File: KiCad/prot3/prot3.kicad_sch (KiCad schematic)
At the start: 198 parts, among them J1 Conn_01x02_Socket, J2 LED_SW, J3 Conn_01x04_Socket, Q1 Q_Photo_NPN, Q10 Q_Photo_NPN, Q11 Q_Photo_NPN, Q12 Q_Photo_NPN, Q13 Q_Photo_NPN, Q14 Q_Photo_NPN, Q15 Q_Photo_NPN, Q16 Q_Photo_NPN, Q17 Q_Photo_NPN, Q18 Q_Photo_NPN, Q19 Q_Photo_NPN, Q2 Q_Photo_NPN, Q20 Q_Photo_NPN, Q21 Q_Photo_NPN, Q22 Q_Photo_NPN, Q23 Q_Photo_NPN, Q24 Q_Photo_NPN, Q25 Q_Photo_NPN, Q26 Q_Photo_NPN, Q27 Q_Photo_NPN, Q28 Q_Photo_NPN, Q29 Q_Photo_NPN, Q3 Q_Photo_NPN, Q30 Q_Photo_NPN, Q31 Q_Photo_NPN, Q32 Q_Photo_NPN, Q4 Q_Photo_NPN, Q5 Q_Photo_NPN, Q6 Q_Photo_NPN, Q7 Q_Photo_NPN, Q8 Q_Photo_NPN, Q9 Q_Photo_NPN, U1 LM339, U2 LM339, U3 LM339, U4 LM339, U5 LM339, U6 LM339, U7 LM339, U8 LM339

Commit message: コンパレーター割当て途中
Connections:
- net 1A: now also Q31.2 (E), Rs31.1
- net 1B: now also Q32.2 (E), Rs32.1
- net 1C: now also Q2.2 (E), Rs2.1
- net 1D: now also Q1.2 (E), Rs1.1
- net 2A: now also Q4.2 (E), Rs4.1
- net 2B: now also Q3.2 (E), Rs3.1
- net 2C: now also Q6.2 (E), Rs6.1
- net 2D: now also Q5.2 (E), Rs5.1
- net 3A: now also Q7.2 (E), Rs7.1
- net 3B: now also Q8.2 (E), Rs8.1
- net 3C: now also Q10.2 (E), Rs10.1
- net 3D: now also Q9.2 (E), Rs9.1
- net 4A: now also Q11.2 (E), Rs11.1
- net 4B: now also Q12.2 (E), Rs12.1
- net 4C: now also Q14.2 (E), Rs14.1
- net 4D: now also Q13.2 (E), Rs13.1
- net 5A: now also Q15.2 (E), Rs15.1
- net 5B: now also Q16.2 (E), Rs16.1
- net 5D: now also Q17.2 (E), Rs17.1
- net 6A: now also Q18.2 (E), Rs18.1
- net 6B: now also Q19.2 (E), Rs19.1
- net 6D: now also Q20.2 (E), Rs20.1
- net 7A: now also Q21.2 (E), Rs21.1
- net 7B: now also Q22.2 (E), Rs22.1
- net 7C: now also Q24.2 (E), Rs24.1
- net 7D: now also Q23.2 (E), Rs23.1
- net 8A: now also Q25.2 (E), Q28.2 (E), Rs25.1, Rs28.1
- net 8B: now also Q26.2 (E), Q27.2 (E), Rs26.1, Rs27.1
- net 8C: now also Q30.2 (E), Rs30.1
- net 8D: now also Q29.2 (E), Rs29.1
- net GND: no longer C13.1, D1.2 (A), D10.2 (A), D11.2 (A), D12.2 (A), D13.2 (A), D14.2 (A), D15.2 (A), D16.2 (A), D17.2 (A), D18.2 (A), D19.2 (A), D2.2 (A), D20.2 (A), D21.2 (A), D22.2 (A), D23.2 (A), D24.2 (A), D25.2 (A), D26.2 (A), D27.2 (A), D28.2 (A), D29.2 (A), D3.2 (A), D30.2 (A), D31.2 (A), D32.2 (A), D4.2 (A), D5.2 (A), D6.2 (A), D7.2 (A), D8.2 (A), D9.2 (A), J1.1 (Pin_1), J2.3 (Pin_3)
- new net LED_5V: C13.1, D1.2 (A), D10.2 (A), D11.2 (A), D12.2 (A), D13.2 (A), D14.2 (A), D15.2 (A), D16.2 (A), D17.2 (A), D18.2 (A), D19.2 (A), D2.2 (A), D20.2 (A), D21.2 (A), D22.2 (A), D23.2 (A), D24.2 (A), D25.2 (A), D26.2 (A), D27.2 (A), D28.2 (A), D29.2 (A), D3.2 (A), D30.2 (A), D31.2 (A), D32.2 (A), D4.2 (A), D5.2 (A), D6.2 (A), D7.2 (A), D8.2 (A), D9.2 (A), J1.1 (Pin_1), J2.3 (Pin_3)

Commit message: conp+一周、センサーch割当てまで
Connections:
- net 1A: now also Q32.2 (E), Rs32.1; no longer Q31.2 (E), Rs31.1
- net 1B: now also Q31.2 (E), Rs31.1; no longer Q32.2 (E), Rs32.1
- net 3A: now also Q8.2 (E), Rs8.1; no longer Q7.2 (E), Rs7.1
- net 3B: now also Q7.2 (E), Rs7.1; no longer Q8.2 (E), Rs8.1
- net 4A: now also Q12.2 (E), Rs12.1; no longer Q11.2 (E), Rs11.1
- net 4B: now also Q11.2 (E), Rs11.1; no longer Q12.2 (E), Rs12.1
- net 5A: now also Q16.2 (E), Rs16.1; no longer Q15.2 (E), Rs15.1
- net 5B: now also Q15.2 (E), Rs15.1; no longer Q16.2 (E), Rs16.1
- net 5C: now also Q18.2 (E), Rs18.1
- net 6A: now also Q20.2 (E), Rs20.1; no longer Q18.2 (E), Rs18.1
- net 6C: now also Q22.2 (E), Rs22.1
- net 6D: now also Q21.2 (E), Rs21.1; no longer Q20.2 (E), Rs20.1
- net 7A: now also Q24.2 (E), Rs24.1; no longer Q21.2 (E), Rs21.1
- net 7B: now also Q23.2 (E), Rs23.1; no longer Q22.2 (E), Rs22.1
- net 7C: now also Q26.2 (E), Rs26.1; no longer Q24.2 (E), Rs24.1
- net 7D: now also Q25.2 (E), Rs25.1; no longer Q23.2 (E), Rs23.1
- net 8A: no longer Q25.2 (E), Rs25.1
- net 8B: no longer Q26.2 (E), Rs26.1
- net LED_5V: now also J2.1 (Pin_1); no longer J1.1 (Pin_1), J2.3 (Pin_3)
- net at J2.2 (Pin_2): now also J1.1 (Pin_1), J2.3 (Pin_3); no longer J2.1 (Pin_1)
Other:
- moved on the sheet: C13, J2

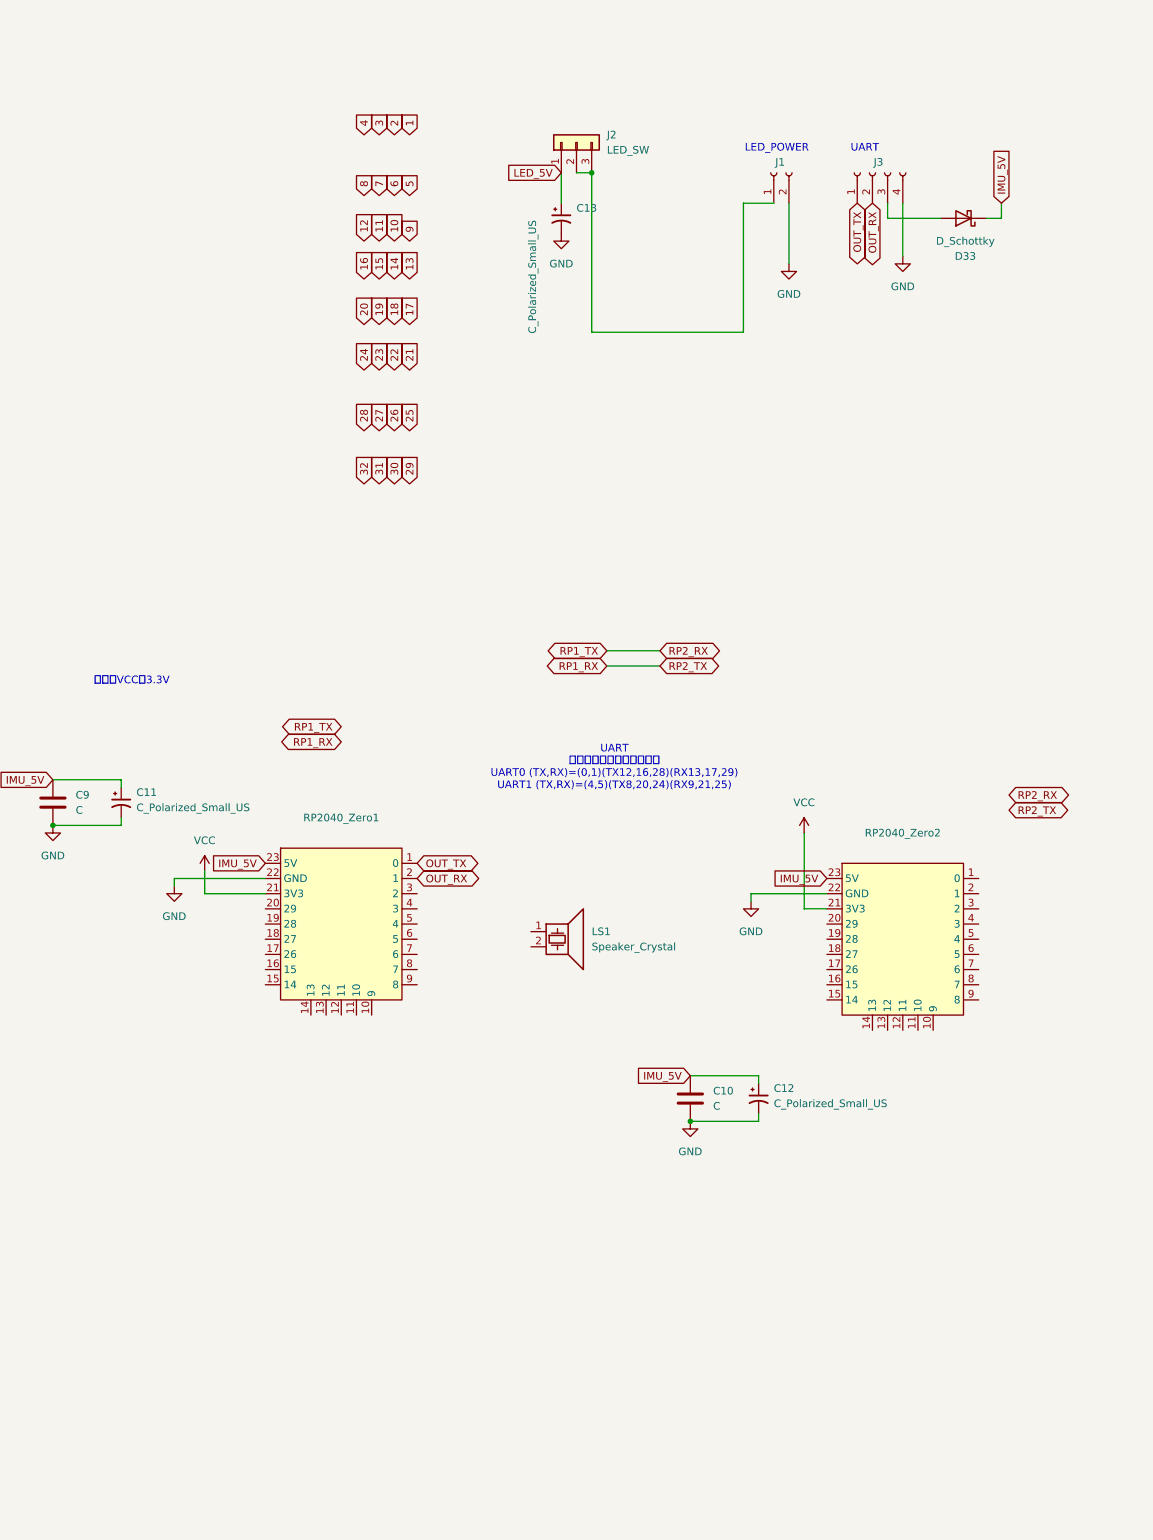
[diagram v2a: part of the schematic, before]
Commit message: IMU用コンデンサ変更
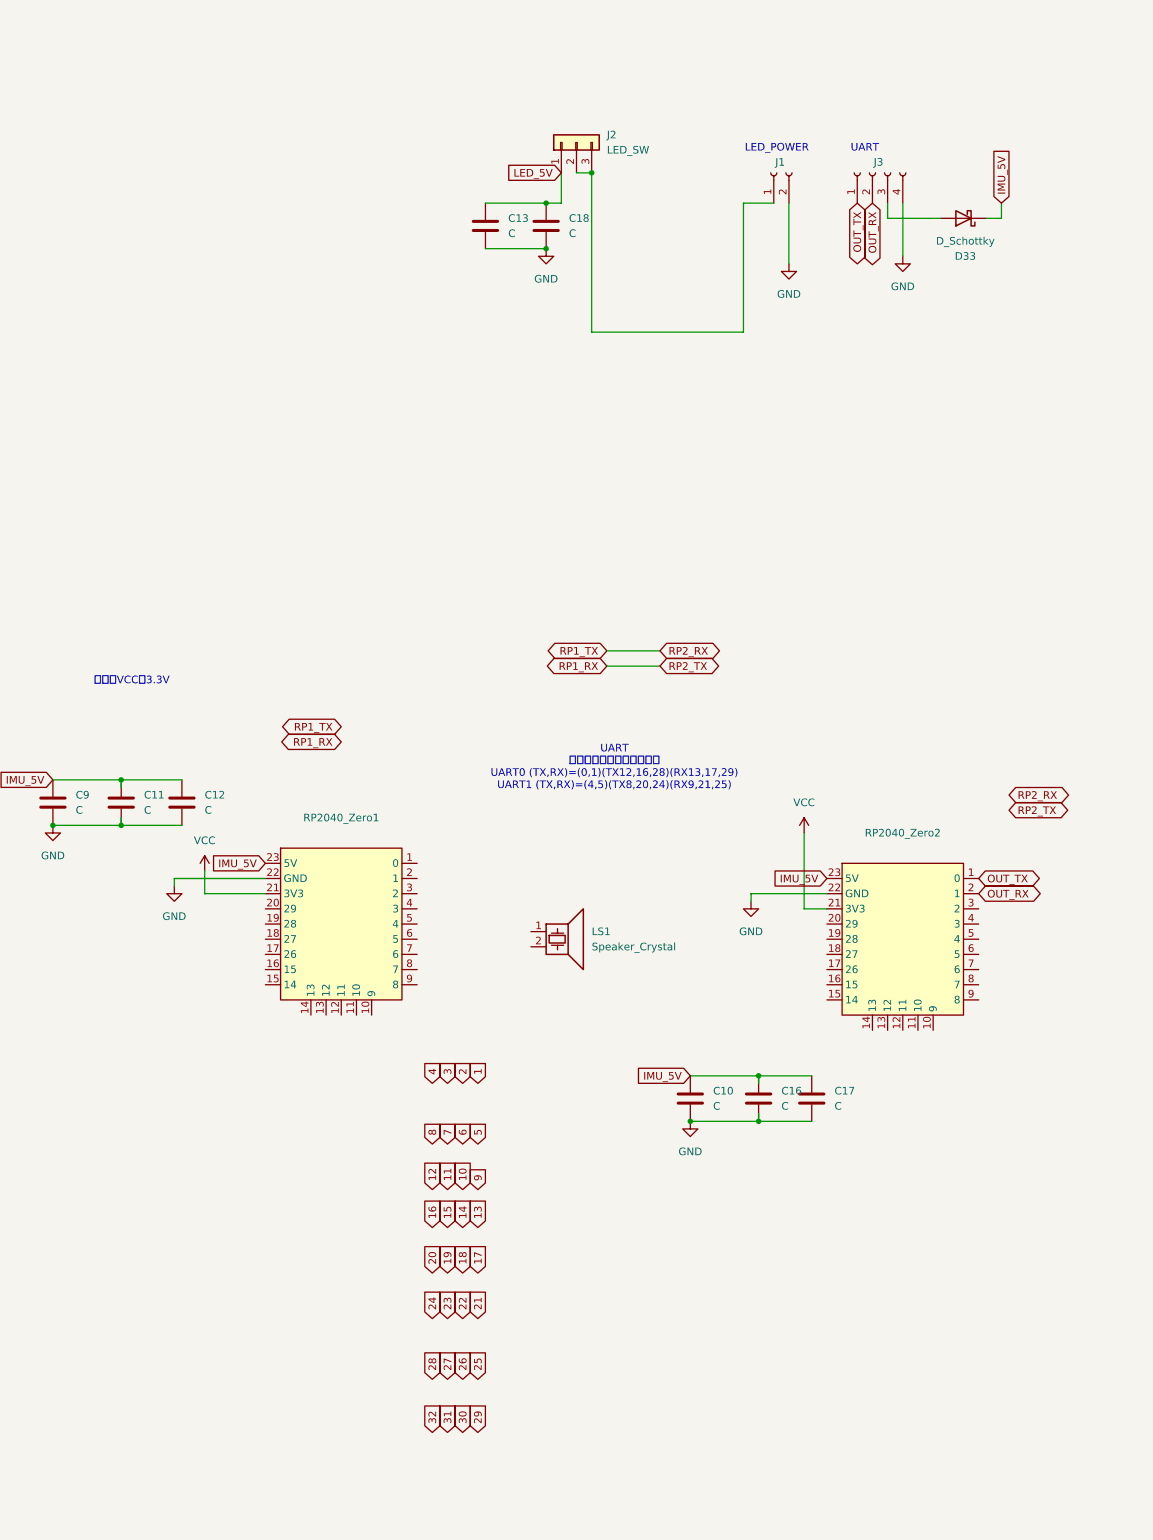
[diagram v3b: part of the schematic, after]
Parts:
- removed C11, C12, C13: C_Polarized_Small_US, Capacitor_THT:C_Radial_D8.0mm_H11.5mm_P3.50mm, symbol Device:C_Polarized_Small_US
- added C11, C12, C13, C16, C17, C18: C, Capacitor_SMD:C_0603_1608Metric_Pad1.08x0.95mm_HandSolder, symbol Device:C
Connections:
- net GND: now also C11.2, C12.2, C13.2, C16.2, C17.2, C18.2
- net IMU_5V: now also C11.1, C12.1, C16.1, C17.1
- net LED_5V: now also C13.1, C18.1
- net OUT_RX: now also RP2040_Zero2.2 (1); no longer RP2040_Zero1.2 (1)
- net OUT_TX: now also RP2040_Zero2.1 (0); no longer RP2040_Zero1.1 (0)

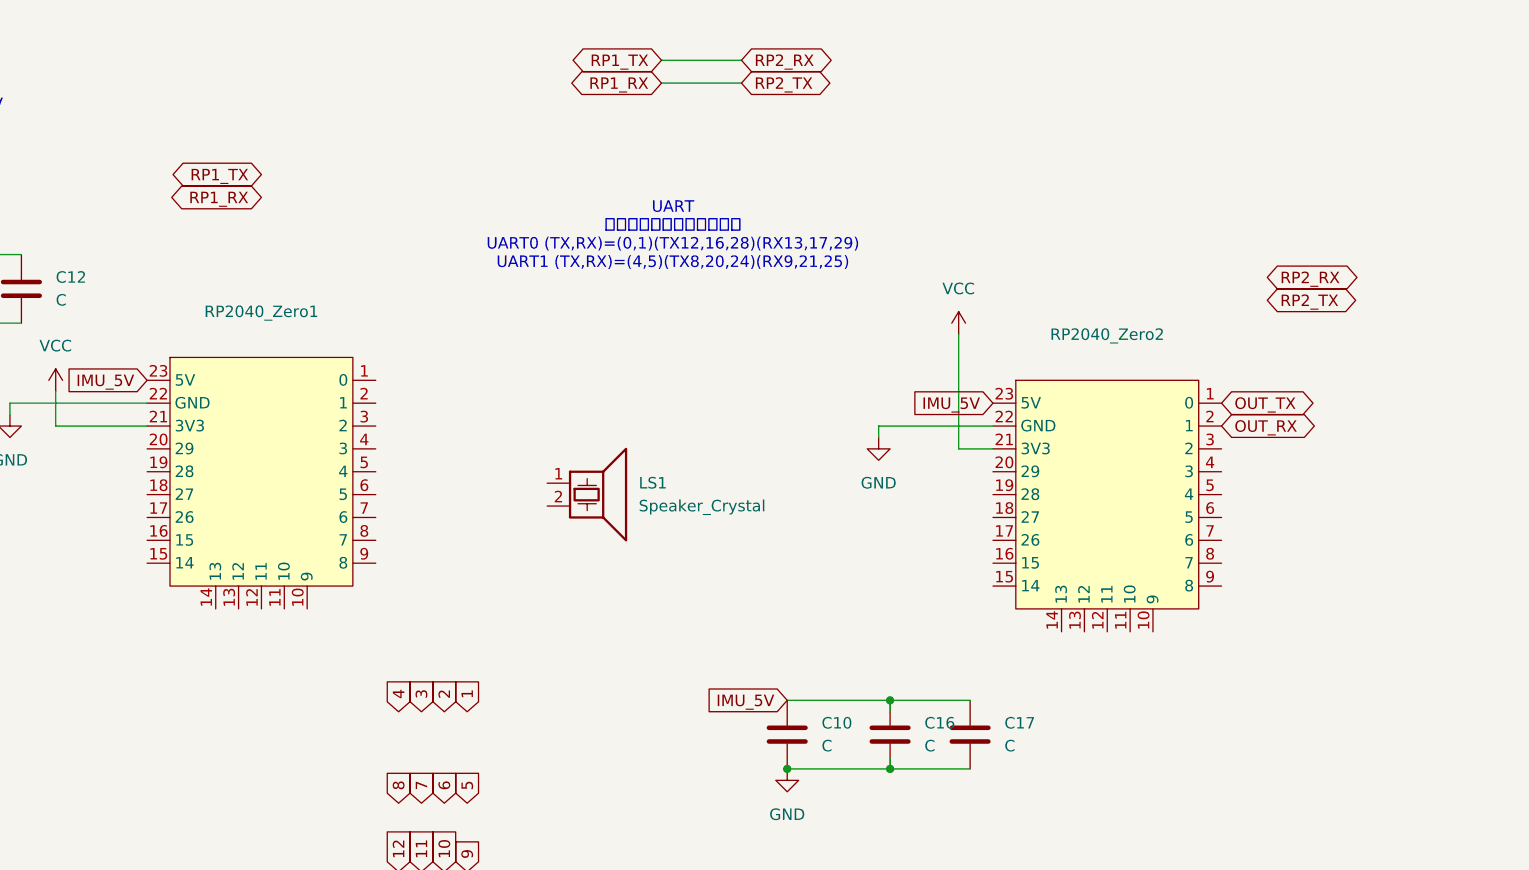
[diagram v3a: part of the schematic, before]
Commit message: コンパレーターデジタル信号配線開始
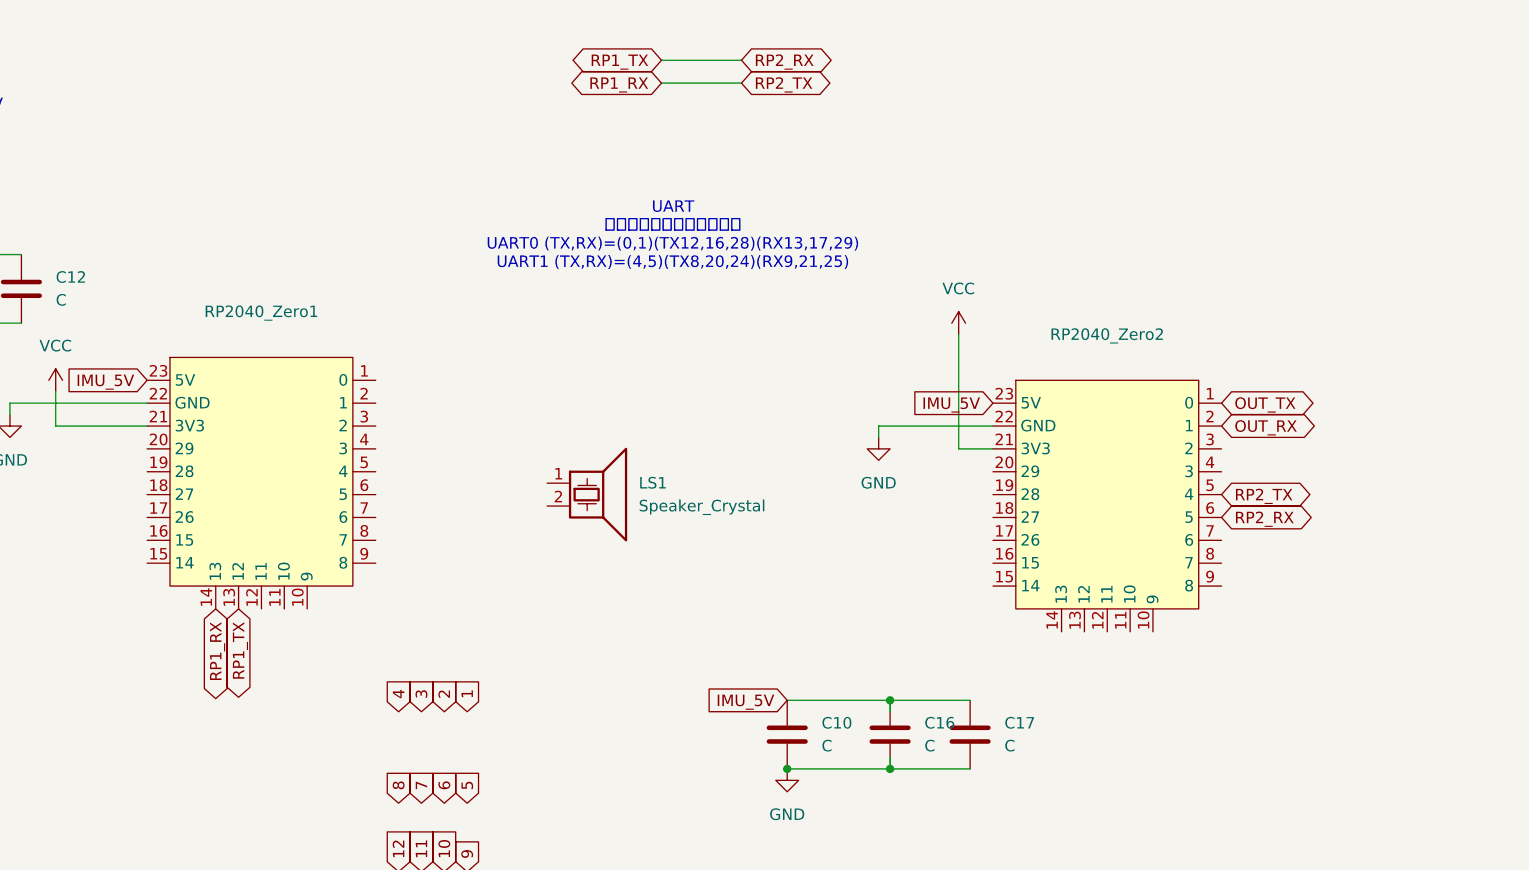
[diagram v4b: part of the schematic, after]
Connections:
- net RP1_RX: now also RP2040_Zero1.14 (13), RP2040_Zero2.5 (4)
- net RP1_TX: now also RP2040_Zero1.13 (12), RP2040_Zero2.6 (5)
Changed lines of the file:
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@@
 	(global_label "RP2_RX"
 		(shape bidirectional)
-		(at 212.09 275.59 0)
-		(fields_autoplaced yes)
-		(effects
-			(font
-				(size 1.27 1.27)
-			)
-			(justify left)
-		)
-		(property "Intersheetrefs" "${INTERSHEET_REFS}"
-			(at 223.3831 275.59 0)
+		(at 207.01 302.26 0)
+		(fields_autoplaced yes)
+		(effects
+			(font
+				(size 1.27 1.27)
+			)
+			(justify left)
+		)
+		(property "Intersheetrefs" "${INTERSHEET_REFS}"
+			(at 218.3031 302.26 0)
 			(effects
 				(font
@@
 	(global_label "RP2_TX"
 		(shape bidirectional)
-		(at 212.09 278.13 0)
-		(fields_autoplaced yes)
-		(effects
-			(font
-				(size 1.27 1.27)
-			)
-			(justify left)
-		)
-		(property "Intersheetrefs" "${INTERSHEET_REFS}"
-			(at 223.0807 278.13 0)
+		(at 207.01 299.72 0)
+		(fields_autoplaced yes)
+		(effects
+			(font
+				(size 1.27 1.27)
+			)
+			(justify left)
+		)
+		(property "Intersheetrefs" "${INTERSHEET_REFS}"
+			(at 218.0007 299.72 0)
 			(effects
 				(font
@@
 	(global_label "RP1_TX"
 		(shape bidirectional)
-		(at 100.33 264.16 180)
+		(at 97.79 312.42 270)
 		(fields_autoplaced yes)
 		(effects
@@
 		)
 		(property "Intersheetrefs" "${INTERSHEET_REFS}"
-			(at 89.3393 264.16 0)
+			(at 97.79 323.4107 90)
 			(effects
 				(font
@@
 	(global_label "RP1_RX"
 		(shape bidirectional)
-		(at 100.33 266.7 180)
+		(at 95.25 312.42 270)
 		(fields_autoplaced yes)
 		(effects
@@
 		)
 		(property "Intersheetrefs" "${INTERSHEET_REFS}"
-			(at 89.0369 266.7 0)
-			(effects
-				(font
+			(at 95.25 323.7131 90)
+			(effects
+				(font

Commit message: バイブコーディングはうんこ
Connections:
- net 1: now also RP2040_Zero1.20 (29)
- net 2: now also RP2040_Zero1.19 (28)
- net 3: now also RP2040_Zero1.17 (26)
- net 4: now also RP2040_Zero1.18 (27)
- net 5: now also RP2040_Zero1.16 (15)
- net 6: now also RP2040_Zero1.15 (14)
- net 7: now also RP2040_Zero1.10 (9)
- net 8: now also RP2040_Zero1.11 (10)
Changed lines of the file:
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@@
 		)
 	)
+	(global_label "8"
+		(shape input)
+		(at 102.87 312.42 270)
+		(fields_autoplaced yes)
+		(effects
+			(font
+				(size 1.27 1.27)
+			)
+			(justify right)
+		)
+		(property "Intersheetrefs" "${INTERSHEET_REFS}"
+			(at 102.87 316.6147 90)
+			(effects
+				(font
+					(size 1.27 1.27)
+				)
+				(justify right)
+				(hide yes)
+			)
+		)
+	)
 	(global_label "LED_5V"
 		(shape input)
@@
 		)
 	)
+	(global_label "6"
+		(shape input)
+		(at 87.63 307.34 180)
+		(fields_autoplaced yes)
+		(effects
+			(font
+				(size 1.27 1.27)
+			)
+			(justify right)
+		)
+		(property "Intersheetrefs" "${INTERSHEET_REFS}"
+			(at 83.4353 307.34 0)
+			(effects
+				(font
+					(size 1.27 1.27)
+				)
+				(justify right)
+				(hide yes)
+			)
+		)
+	)
 	(global_label "conp_+"
 		(shape bidirectional)
@@
 		)
 	)
+	(global_label "4"
+		(shape input)
+		(at 87.63 299.72 180)
+		(fields_autoplaced yes)
+		(effects
+			(font
+				(size 1.27 1.27)
+			)
+			(justify right)
+		)
+		(property "Intersheetrefs" "${INTERSHEET_REFS}"
+			(at 83.4353 299.72 0)
+			(effects
+				(font
+					(size 1.27 1.27)
+				)
+				(justify right)
+				(hide yes)
+			)
+		)
+	)
 	(global_label "2B"
 		(shape input)
@@
 	(global_label "7"
 		(shape input)
+		(at 105.41 312.42 270)
+		(fields_autoplaced yes)
+		(effects
+			(font
+				(size 1.27 1.27)
+			)
+			(justify right)
+		)
+		(property "Intersheetrefs" "${INTERSHEET_REFS}"
+			(at 105.41 316.6147 90)
+			(effects
+				(font
+					(size 1.27 1.27)
+				)
+				(justify right)
+				(hide yes)
+			)
+		)
+	)
+	(global_label "7"
+		(shape input)
 		(at 647.7 256.54 90)
 		(fields_autoplaced yes)
@@
 		)
 	)
+	(global_label "2"
+		(shape input)
+		(at 87.63 297.18 180)
+		(fields_autoplaced yes)
+		(effects
+			(font
+				(size 1.27 1.27)
+			)
+			(justify right)
+		)
+		(property "Intersheetrefs" "${INTERSHEET_REFS}"
+			(at 83.4353 297.18 0)
+			(effects
+				(font
+					(size 1.27 1.27)
+				)
+				(justify right)
+				(hide yes)
+			)
+		)
+	)
 	(global_label "IMU_5V"
 		(shape input)
@@
 		)
 	)
+	(global_label "3"
+		(shape input)
+		(at 87.63 302.26 180)
+		(fields_autoplaced yes)
+		(effects
+			(font
+				(size 1.27 1.27)
+			)
+			(justify right)
+		)
+		(property "Intersheetrefs" "${INTERSHEET_REFS}"
+			(at 83.4353 302.26 0)
+			(effects
+				(font
+					(size 1.27 1.27)
+				)
+				(justify right)
+				(hide yes)
+			)
+		)
+	)
 	(global_label "5D"
 		(shape input)
@@
 	(global_label "1"
 		(shape input)
-		(at 123.19 323.85 90)
+		(at 87.63 294.64 180)
 		(fields_autoplaced yes)
 		(effects
@@
 				(size 1.27 1.27)
 			)
-			(justify left)
+			(justify right)
 		)
 		(property "Intersheetrefs" "${INTERSHEET_REFS}"
-			(at 123.19 319.6553 90)
+			(at 83.4353 294.64 0)
 			(effects
 				(font
 					(size 1.27 1.27)
 				)
-				(justify left)
+				(justify right)
 				(hide yes)
 			)
@@
 				(hide yes)
 			)
+		)
+	)
+	(global_label "5"
+		(shape input)
+		(at 87.63 304.8 180)
+		(fields_autoplaced yes)
+		(effects
+			(font
+				(size 1.27 1.27)
+			)
+			(justify right)
+		)
+		(property "Intersheetrefs" "${INTERSHEET_REFS}"
+			(at 83.4353 304.8 0)
+			(effects
+				(font
+					(size 1.27 1.27)
+				)
+				(justify right)
+				(hide yes)
+			)
